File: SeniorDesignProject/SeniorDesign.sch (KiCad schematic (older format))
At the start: 24 parts, among them J1 RJ45(LoadCells), J2 RJ45(Accelerometer), J3 PICkit3, J5 ID-12LA Header, J6 XBEE Header, J7 7-Segment Display, P7 Power 1, U1 INA827, U2 LM1117-3.3, U3 ICL7660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

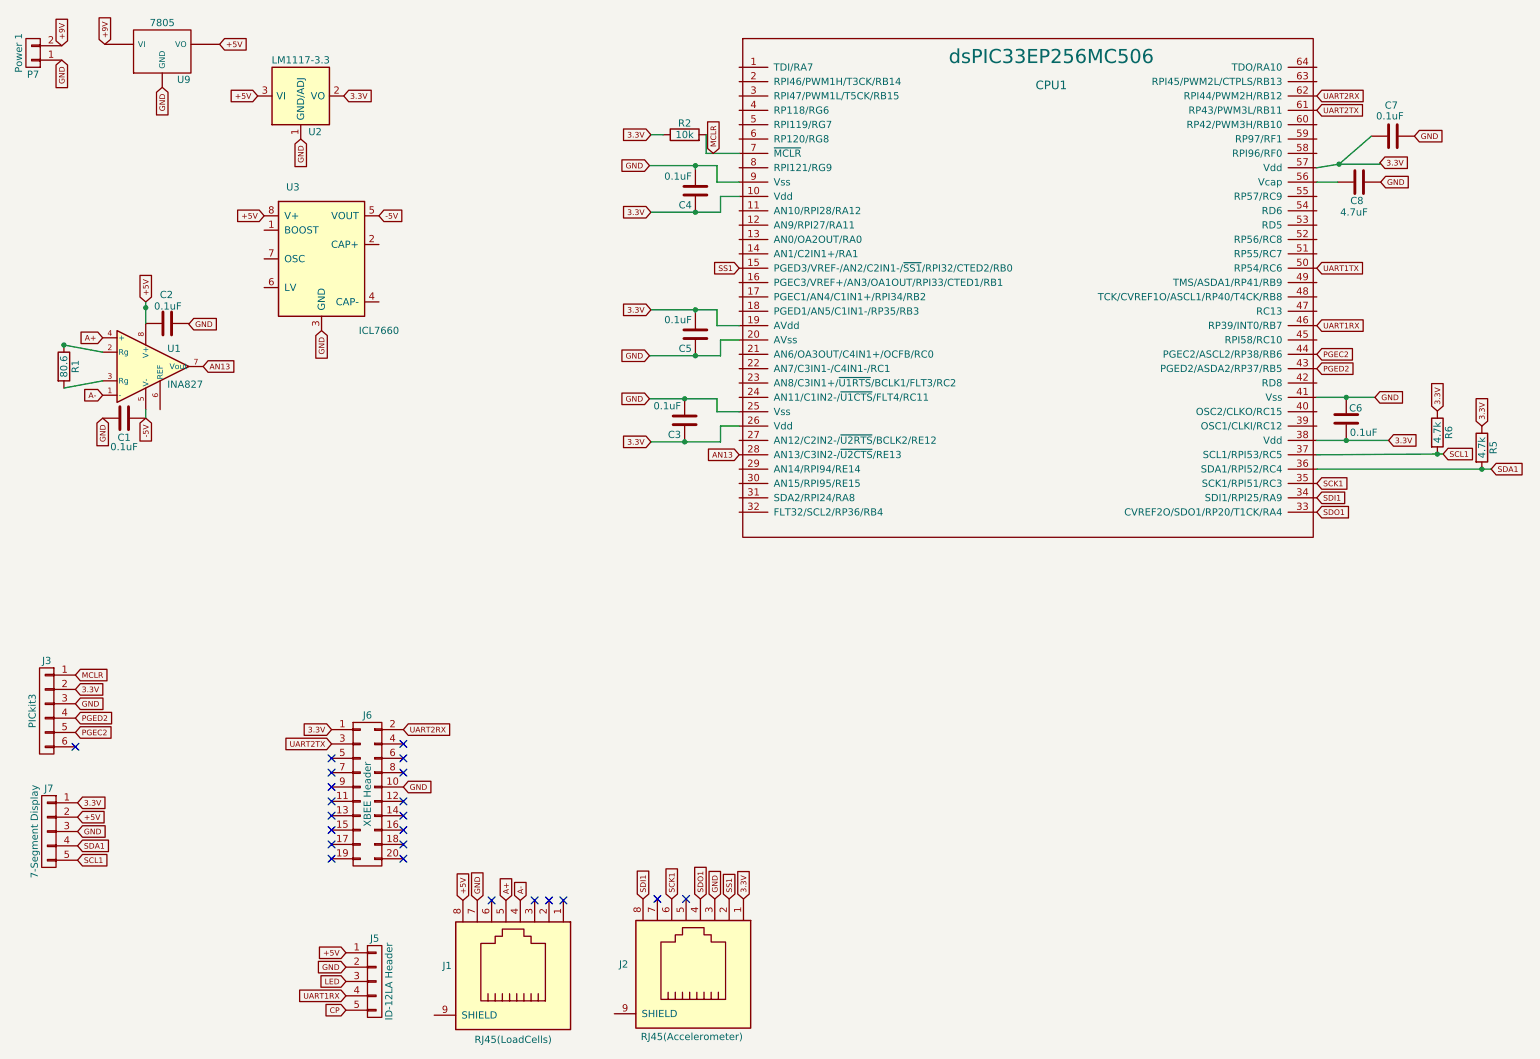
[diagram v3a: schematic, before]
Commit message: Updates to accelerometer board and main board
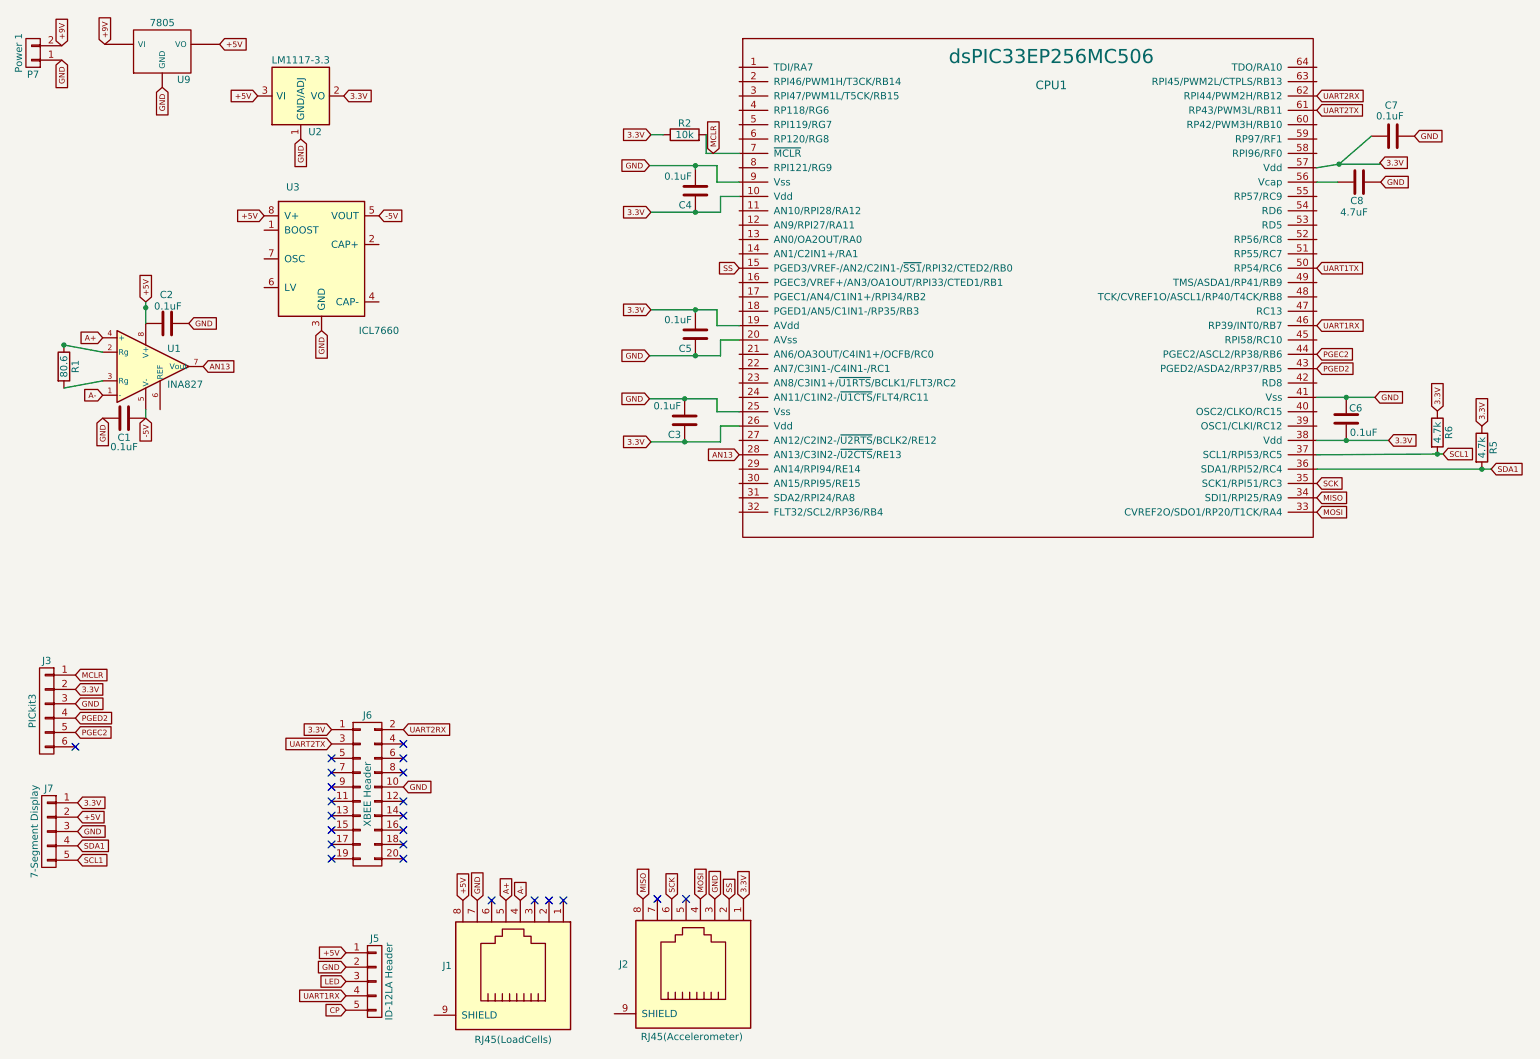
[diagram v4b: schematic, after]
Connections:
- net GND: now also C2.2
- net SCK1 renamed SCK
- net SDI1 renamed MISO
- net SDO1 renamed MOSI
- net SS1 renamed SS
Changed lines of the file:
@@
 	0    -1   -1   0
 $EndComp
-Text GLabel 1805 2685 2    39   Input ~ 0
+Text GLabel 1805 2680 2    39   Input ~ 0
 GND
 Text GLabel 1205 3340 3    39   Input ~ 0
@@
 $EndComp
 Text GLabel 5640 2295 0    39   Input ~ 0
-SS1
+SS
 Text GLabel 9665 3995 2    39   Input ~ 0
-SDO1
+MOSI
 Text GLabel 9665 3895 2    39   Input ~ 0
-SDI1
+MISO
 Text GLabel 9665 3795 2    39   Input ~ 0
-SCK1
+SCK
 Text GLabel 5670 6690 1    39   Input ~ 0
 3.3V
 Text GLabel 5570 6690 1    39   Input ~ 0
-SS1
+SS
 Text GLabel 5370 6690 1    39   Input ~ 0
-SDO1
+MOSI
 Text GLabel 5170 6690 1    39   Input ~ 0
-SCK1
+SCK
 Text GLabel 4970 6690 1    39   Input ~ 0
-SDI1
+MISO
 NoConn ~ 5070 6690
 NoConn ~ 5270 6690

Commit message: Updates to main board
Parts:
- added C10, C9: 10u, Capacitors_THT:CP_Radial_D5.0mm_P2.00mm, symbol C
- C8: footprint Capacitors_SMD:CP_Elec_4x4.5 -> Capacitors_THT:CP_Radial_D5.0mm_P2.00mm
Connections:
- net -5V: now also C10.1
- net CP: now also CPU1.49 (TMS/ASDA1/RP41/RB9)
- net GND: now also C10.2
- net LED: now also CPU1.47 (RC13)
- net at U3.2 (CAP+): now also C9.1
- net at U3.4 (CAP-): now also C9.2
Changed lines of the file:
@@
 F 0 "C8" V 10090 1665 50  0000 L CNN
 F 1 "4.7uF" V 10170 1635 50  0000 L CNN
-F 2 "Capacitors_SMD:CP_Elec_4x4.5" H 9998 1545 50  0001 C CNN
+F 2 "Capacitors_THT:CP_Radial_D5.0mm_P2.00mm" H 9998 1545 50  0001 C CNN
 F 3 "" H 9960 1695 50  0001 C CNN
 	1    9960 1695
@@
 Text GLabel 2330 1930 0    39   Input ~ 0
 +5V
-Text GLabel 3130 1930 2    39   Input ~ 0
+Text GLabel 3210 1930 2    39   Input ~ 0
 -5V
 Text GLabel 1620 1035 3    39   Input ~ 0
@@
 Text GLabel 5460 1495 1    39   Input ~ 0
 MCLR
+$Comp
+L C C9
+U 1 1 58D03AE9
+P 3130 2280
+F 0 "C9" H 3155 2380 50  0000 L CNN
+F 1 "10u" H 3155 2180 50  0000 L CNN
+F 2 "Capacitors_THT:CP_Radial_D5.0mm_P2.00mm" H 3168 2130 50  0001 C CNN
+F 3 "" H 3130 2280 50  0001 C CNN
+	1    3130 2280
+	1    0    0    -1
+$EndComp
+Wire Wire Line
+	3130 2530 3130 2430
+Wire Wire Line
+	3560 2020 3560 2145
+$Comp
+L C C10
+U 1 1 58D03E25
+P 3560 2295
+F 0 "C10" H 3585 2395 50  0000 L CNN
+F 1 "10u" H 3585 2195 50  0000 L CNN
+F 2 "Capacitors_THT:CP_Radial_D5.0mm_P2.00mm" H 3598 2145 50  0001 C CNN
+F 3 "" H 3560 2295 50  0001 C CNN
+	1    3560 2295
+	1    0    0    -1
+$EndComp
+Text GLabel 3560 2445 3    39   Input ~ 0
+GND
+Wire Wire Line
+	3130 1930 3130 2020
+Wire Wire Line
+	3130 2020 3560 2020
+Wire Wire Line
+	3210 1930 3130 1930
+Text GLabel 9665 2595 2    39   Input ~ 0
+LED
+Text GLabel 9665 2395 2    39   Input ~ 0
+CP
 $EndSCHEMATC
